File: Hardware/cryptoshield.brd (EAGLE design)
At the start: 59.7 x 53.3 mm, 48 parts, among them J1 AVR_SPI_PRG_6PTH, Q1 BSS138, Q2 BSS138, Q3 BSS138, U1 74LVC1G04, U2 33mhz, U3 ID-12/20SMD, U4 ARDUINO_R3_SHIELD, U5 ATAES132, U6 AT97SC3204T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

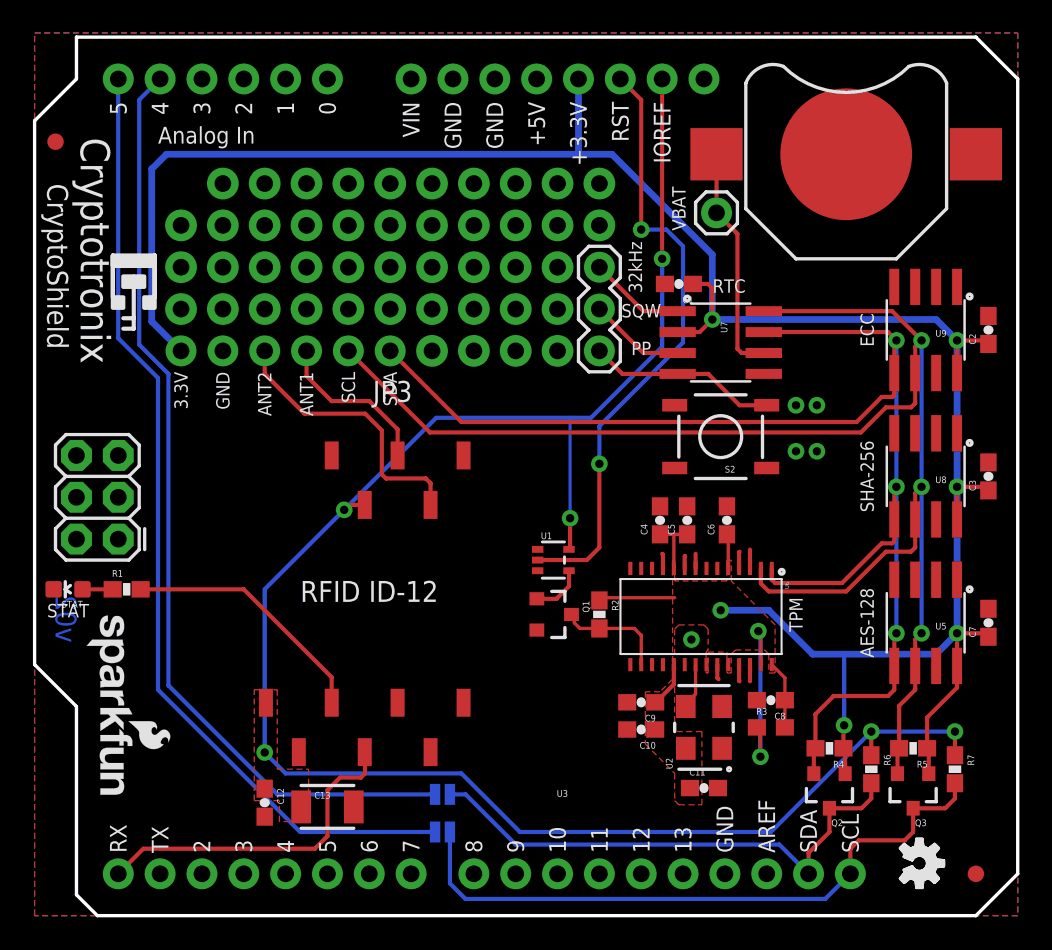
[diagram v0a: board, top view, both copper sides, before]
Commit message: Moved Stat Led away from board re-arranged proto area to conform with I2C standard layout flipped logos to match lable orientation
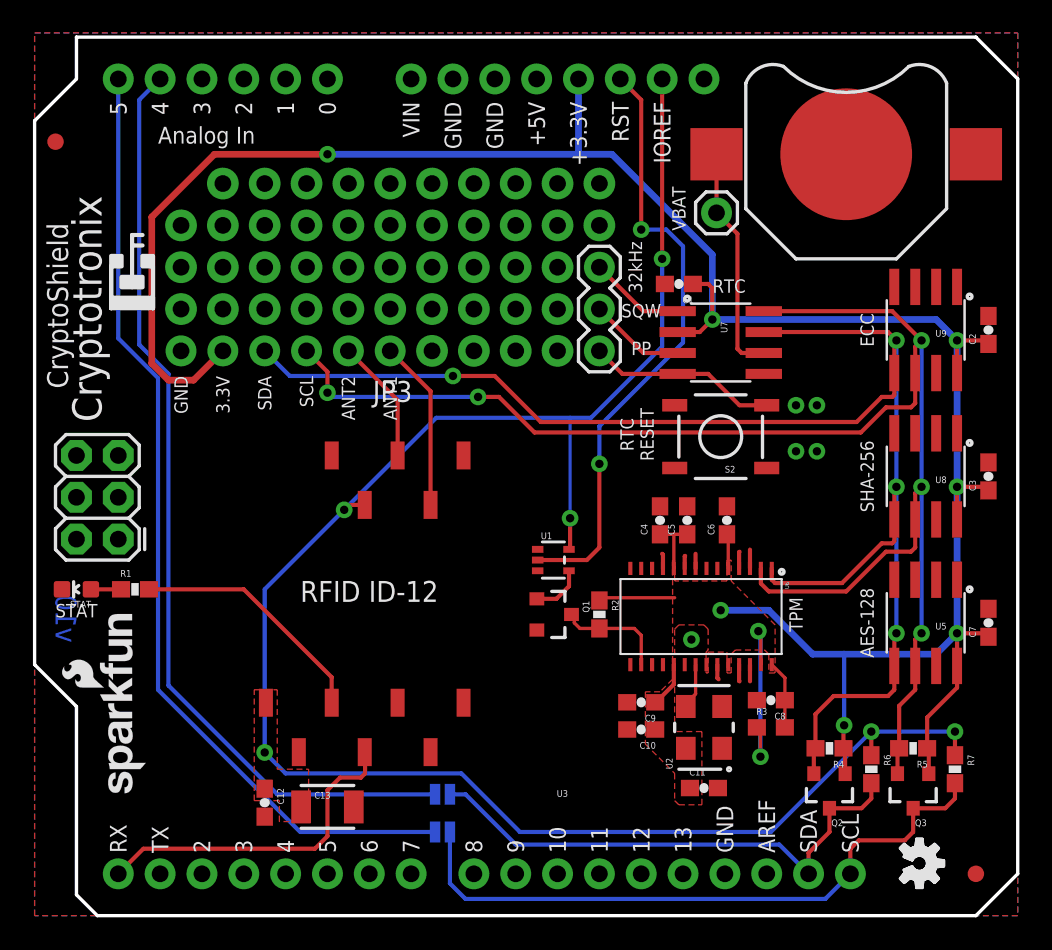
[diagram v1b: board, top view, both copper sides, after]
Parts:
- moved U$101 15.3 mm to (7.87, 21.3), turned to 270 degrees
- moved LOGO3 12.3 mm to (6.86, 6.99), turned to 90 degrees
- moved R1 0.51 mm to (6.10, 19.8)
- moved STAT 0.51 mm to (2.54, 19.8)
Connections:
- net 3.3V: now also JP3.5; no longer JP3.6
- net ANT1: now also JP3.2; no longer JP3.3
- net ANT2: now also JP3.1; no longer JP3.4
- net GND: now also JP3.6; no longer JP3.5
- net SCL: now also JP3.3; no longer JP3.2
- net SDA: now also JP3.4; no longer JP3.1
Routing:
- net SDA: track 87.6 -> 95.3 mm, vias 3 -> 4
- net ANT2: track 17.1 -> 10.4 mm
- net 3.3V: track 156.4 -> 160.1 mm, vias 6 -> 7
- net SCL: track 93.8 -> 97.1 mm, vias 3 -> 5
- net ANT1: track 9.98 -> 7.59 mm
- net N$1: track 15.4 -> 14.9 mm
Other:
- board text added: "RTC RESET"
- board text added: "v10"
- board text removed: "v02"
